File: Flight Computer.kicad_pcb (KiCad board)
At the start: 4 copper layers, 46 x 78.2 mm, 91 parts, among them J1 Conn_01x08, J2 JTAG, Q1 Q_PMOS_GDS, Q2 Q_NMOS_GDS, Q3 Q_NMOS_GDS, Q4 Q_NMOS_GDS, Q5 Q_PMOS_GDS, Q6 Q_PMOS_GDS, SW1 Reset, U1 VXO7803-1000, U2 W25Q16JVSS, U3 W25Q16JVSS, U4 Adafruit_GPS_THT, U5 ADXL345, U6 STM32F303RETx, U7 MAX7375AXR805, U8 BMP280

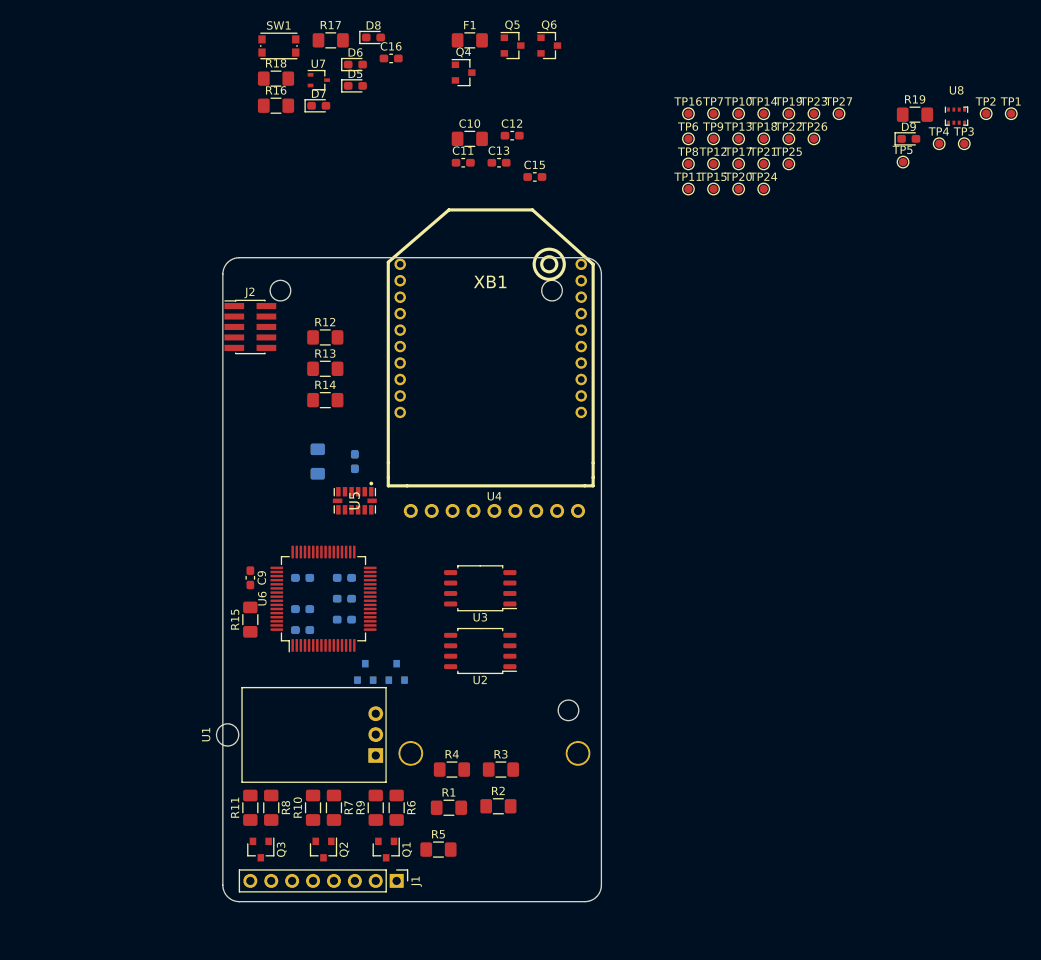
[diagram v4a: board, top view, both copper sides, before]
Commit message: Preliminary component placement
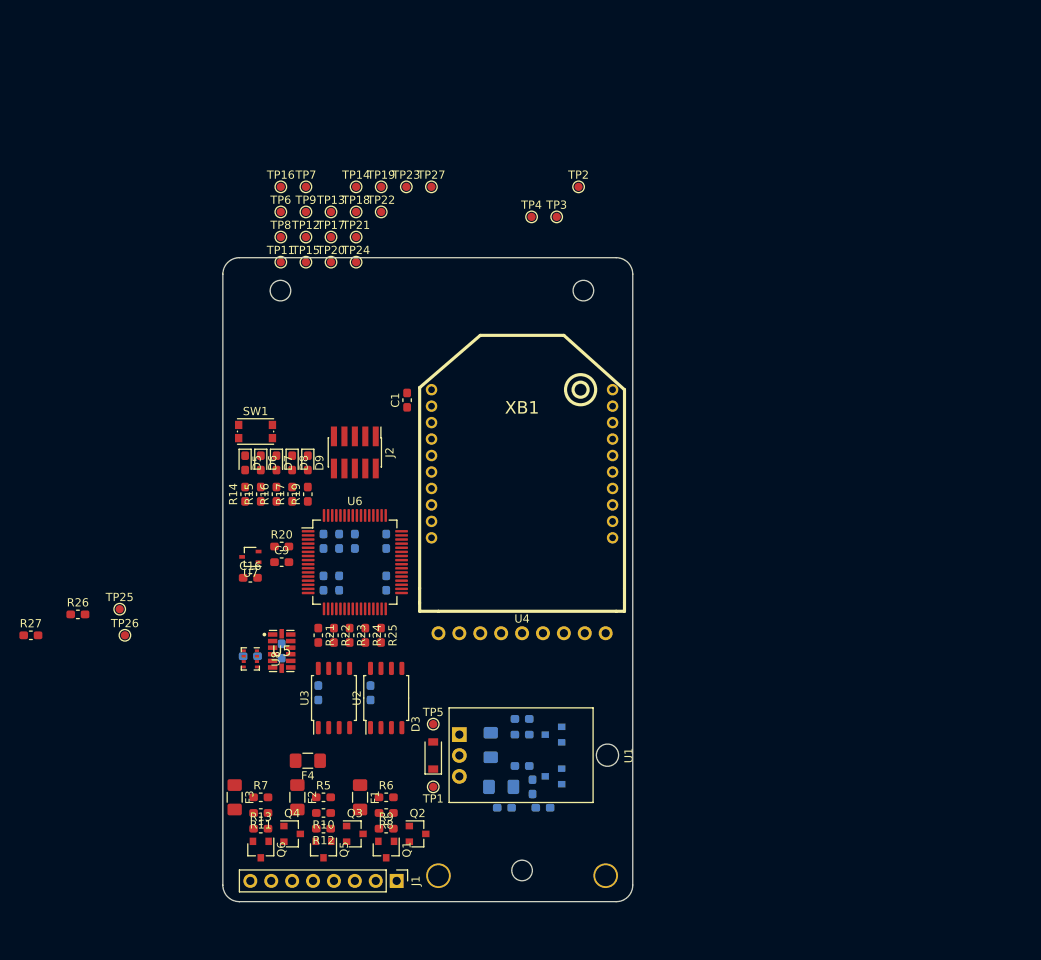
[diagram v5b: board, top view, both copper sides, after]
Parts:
- removed TP10: ACT4, TestPoint:TestPoint_Pad_D1.0mm
- added C14: 1n, Capacitor_SMD:C_0603_1608Metric_Pad1.05x0.95mm_HandSolder, B.Cu at (86.4, 111.8)
- added C17: 1n, Capacitor_SMD:C_0603_1608Metric_Pad1.05x0.95mm_HandSolder, B.Cu at (86.4, 106.0)
- added D3: BAT46, Diode_SMD:D_SOD-123, F.Cu at (75.6, 110.5)
- added F2: 1A Polyfuse, Fuse:Fuse_1206_3216Metric_Pad1.42x1.75mm_HandSolder, F.Cu at (59.1, 115.6)
- added F3: 1A Polyfuse, Fuse:Fuse_1206_3216Metric_Pad1.42x1.75mm_HandSolder, F.Cu at (51.4, 115.6)
- added F4: 3A Polyfuse, Fuse:Fuse_1206_3216Metric_Pad1.42x1.75mm_HandSolder, F.Cu at (60.3, 111.1)
- added R20: 10R, Resistor_SMD:R_0603_1608Metric_Pad1.05x0.95mm_HandSolder, F.Cu at (57.1, 85.1)
- added R21: 10R, Resistor_SMD:R_0603_1608Metric_Pad1.05x0.95mm_HandSolder, F.Cu at (61.6, 95.9)
- added R22: 10R, Resistor_SMD:R_0603_1608Metric_Pad1.05x0.95mm_HandSolder, F.Cu at (63.5, 95.9)
- added R23: 10R, Resistor_SMD:R_0603_1608Metric_Pad1.05x0.95mm_HandSolder, F.Cu at (65.4, 95.9)
- added R24: 10R, Resistor_SMD:R_0603_1608Metric_Pad1.05x0.95mm_HandSolder, F.Cu at (67.3, 95.9)
- added R25: 10R, Resistor_SMD:R_0603_1608Metric_Pad1.05x0.95mm_HandSolder, F.Cu at (69.2, 95.9)
- added R26: 2.2k, Resistor_SMD:R_0603_1608Metric_Pad1.05x0.95mm_HandSolder, F.Cu at (32.4, 93.3)
- added R27: 2.2k, Resistor_SMD:R_0603_1608Metric_Pad1.05x0.95mm_HandSolder, F.Cu at (26.7, 95.9)
- C1: moved to F.Cu
- C10, C11, C12, C13, C15: moved to B.Cu
- F1: value 3A Polyfuse -> 1A Polyfuse
- G1: footprint Flight-Computer:UB-SEDS-Logo -> Flight-Computer:SEDS_logo_soldermask
- R1, R18, R2, R3, R4: footprint Resistor_SMD:R_1206_3216Metric_Pad1.42x1.75mm_HandSolder -> Resistor_SMD:R_0603_1608Metric_Pad1.05x0.95mm_HandSolder; moved to B.Cu
- R10, R11, R12, R13, R5, R6, R7, R8, R9: footprint Resistor_SMD:R_1206_3216Metric_Pad1.42x1.75mm_HandSolder -> Resistor_SMD:R_0603_1608Metric_Pad1.05x0.95mm_HandSolder
- R14, R15, R16, R17, R19: value 1k -> 470R; footprint Resistor_SMD:R_1206_3216Metric_Pad1.42x1.75mm_HandSolder -> Resistor_SMD:R_0603_1608Metric_Pad1.05x0.95mm_HandSolder
- moved U8 108.2 mm to (53.3, 98.8), turned to 270 degrees
- moved TP1 107.8 mm to (75.6, 114.3), turned to 180 degrees
- moved Q6 103.8 mm to (54.6, 121.9), turned to 270 degrees
- moved TP26 103.2 mm to (38.1, 95.9)
- moved Q5 100.4 mm to (62.2, 121.9), turned to 270 degrees
- moved TP25 97.7 mm to (37.5, 92.7)
- moved Q4 94.8 mm to (58.4, 120.0)
- moved F1 92.9 mm to (66.7, 115.6), turned to 270 degrees
- moved TP5 89.0 mm to (75.6, 106.7)
- moved R19 87.0 mm to (60.3, 78.7), turned to 90 degrees
- moved D9 83.0 mm to (60.3, 74.9), turned to 270 degrees
- moved C10 73.7 mm to (82.5, 109.2), turned to 90 degrees
- moved C12 69.9 mm to (67.9, 102.9), turned to 90 degrees
- moved C13 68.1 mm to (61.6, 102.9), turned to 90 degrees
- moved C15 67.7 mm to (53.3, 98.4), turned to 180 degrees
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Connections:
- F1 pad 1: +BATT -> Net-(F1-Pad1)
- Q5 pad 2: Net-(F1-Pad2) -> Net-(F2-Pad2)
- Q6 pad 2: Net-(F1-Pad2) -> Net-(F3-Pad2)
- R12 pad 1: Net-(F1-Pad2) -> Net-(F2-Pad2)
- R13 pad 1: Net-(F1-Pad2) -> Net-(F3-Pad2)
- U6 pad 11: /ACT4 -> (no net)
- U6 pad 30: /SPI2_CS1 -> Net-(R21-Pad1)
- U6 pad 33: /SPI2_CS2 -> Net-(R24-Pad1)
- U6 pad 34: /SPI2_SCK -> Net-(R22-Pad1)
- U6 pad 35: /SPI2_MISO -> Net-(R25-Pad1)
- U6 pad 36: /SPI2_MOSI -> Net-(R23-Pad1)
- U6 pad 5: /MCU/OSC_IN -> Net-(R20-Pad2)
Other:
- board size 46 x 78.2 mm -> 49.8 x 78.2 mm
- board text added: "Flight Computer Rev 4"
- board text removed: "Flight Computer Rev 3"

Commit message: Much more compact component placement Some routing done
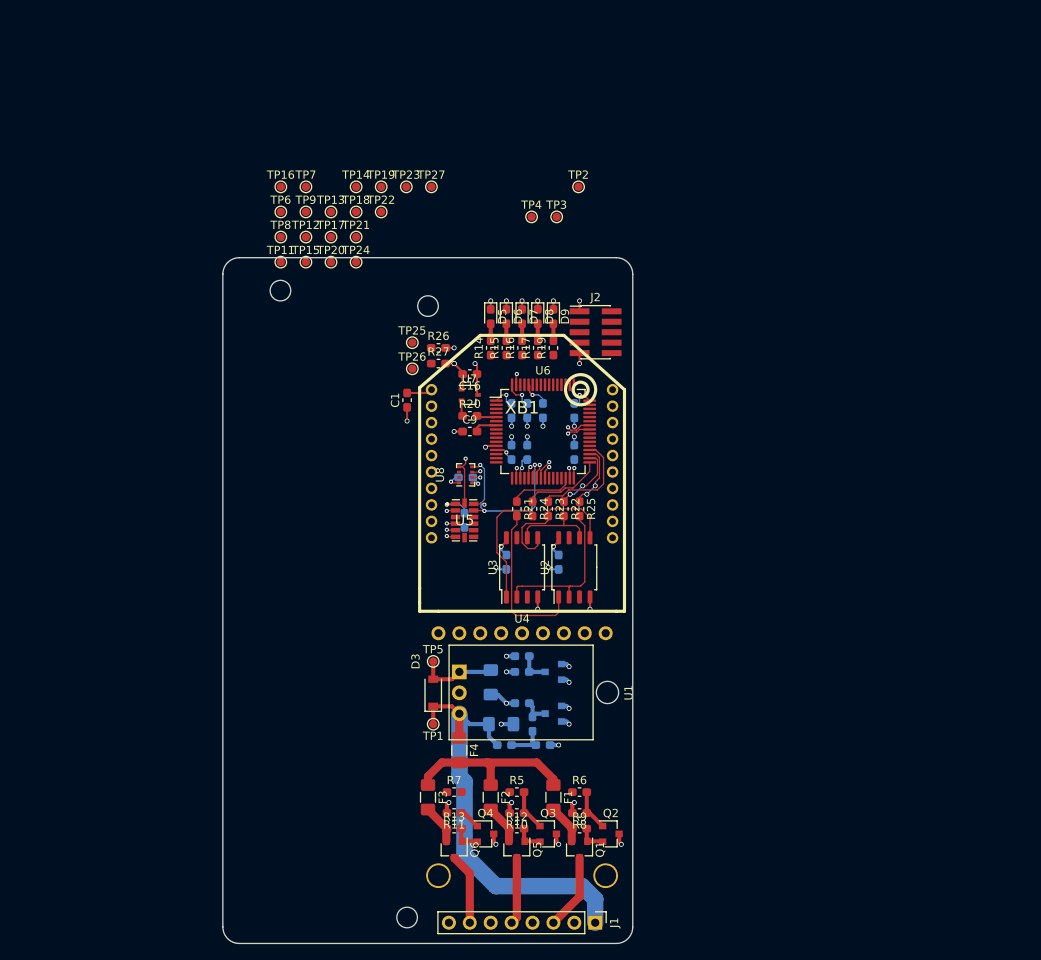
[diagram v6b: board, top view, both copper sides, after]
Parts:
- removed SW1: Reset, Button_Switch_SMD:SW_Push_1P1T_NO_CK_KMR2
- moved R27 59.5 mm to (76.2, 62.9)
- moved R26 54.5 mm to (76.2, 61.0)
- moved TP25 48.1 mm to (73.0, 60.3)
- moved TP26 47.6 mm to (73.0, 63.5)
- moved C16 36.4 mm to (80.0, 64.1), turned to 180 degrees
- moved D5 34.7 mm to (82.5, 57.1)
- moved D6 34.7 mm to (84.5, 57.1)
- moved D7 34.7 mm to (86.4, 57.1)
- moved D8 34.7 mm to (88.3, 57.1)
- moved D9 34.7 mm to (90.2, 57.1)
- moved R14 34.7 mm to (82.5, 61.0)
- moved R15 34.7 mm to (84.5, 61.0)
- moved R16 34.7 mm to (86.4, 61.0)
- moved R17 34.7 mm to (88.3, 61.0)
- moved R19 34.7 mm to (90.2, 61.0)
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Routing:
- net GND: track 0.00 -> 54.8 mm, vias 0 -> 41
- net +BATT: track 0.00 -> 54.1 mm
- net +3V3: track 0.00 -> 52.5 mm, vias 0 -> 19
- net /SPI1_MISO: track 0.00 -> 21.7 mm, vias 0 -> 3
- net Net-(F1-Pad1): track 0.00 -> 21.5 mm
- net /SPI2_CS1: track 0.00 -> 19.8 mm
- net /SPI2_MISO: track 0.00 -> 19.3 mm
- net /SPI2_MOSI: track 0.00 -> 17.8 mm
- net /SPI2_CS2: track 0.00 -> 15.4 mm
- net Net-(R23-Pad1): track 0.00 -> 13.2 mm
- net Net-(R24-Pad1): track 0.00 -> 10.4 mm
- net /SPI2_SCK: track 0.00 -> 10.0 mm
- net /DROGUE_POW: track 0.00 -> 9.21 mm
- net /AUX1_POW: track 0.00 -> 8.68 mm
- net Net-(R22-Pad1): track 0.00 -> 8.35 mm, vias 0 -> 2
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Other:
- board size 49.8 x 78.2 mm -> 49.8 x 83.3 mm
- net class Default: clearance 0.2 -> 0.089; trace_width 0.1524 -> 0.089
- rule trace_clearance: 0.2 -> 0.089
- rule trace_min: 0.1524 -> 0.089
- rule via_min_drill: 0.254 -> 0.2
- rule via_min_size: 0.508 -> 0.45

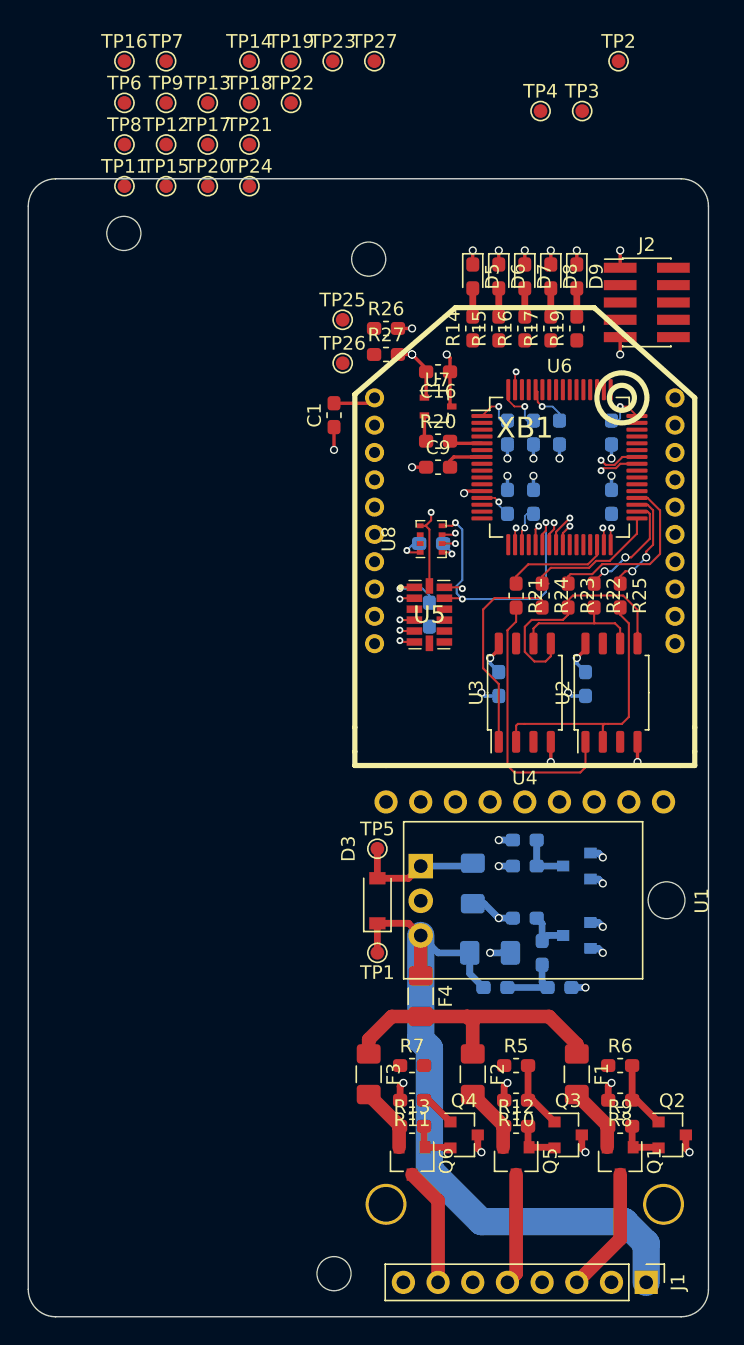
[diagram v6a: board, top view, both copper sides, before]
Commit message: Routing complete Removed some test points (couldn't easily place)
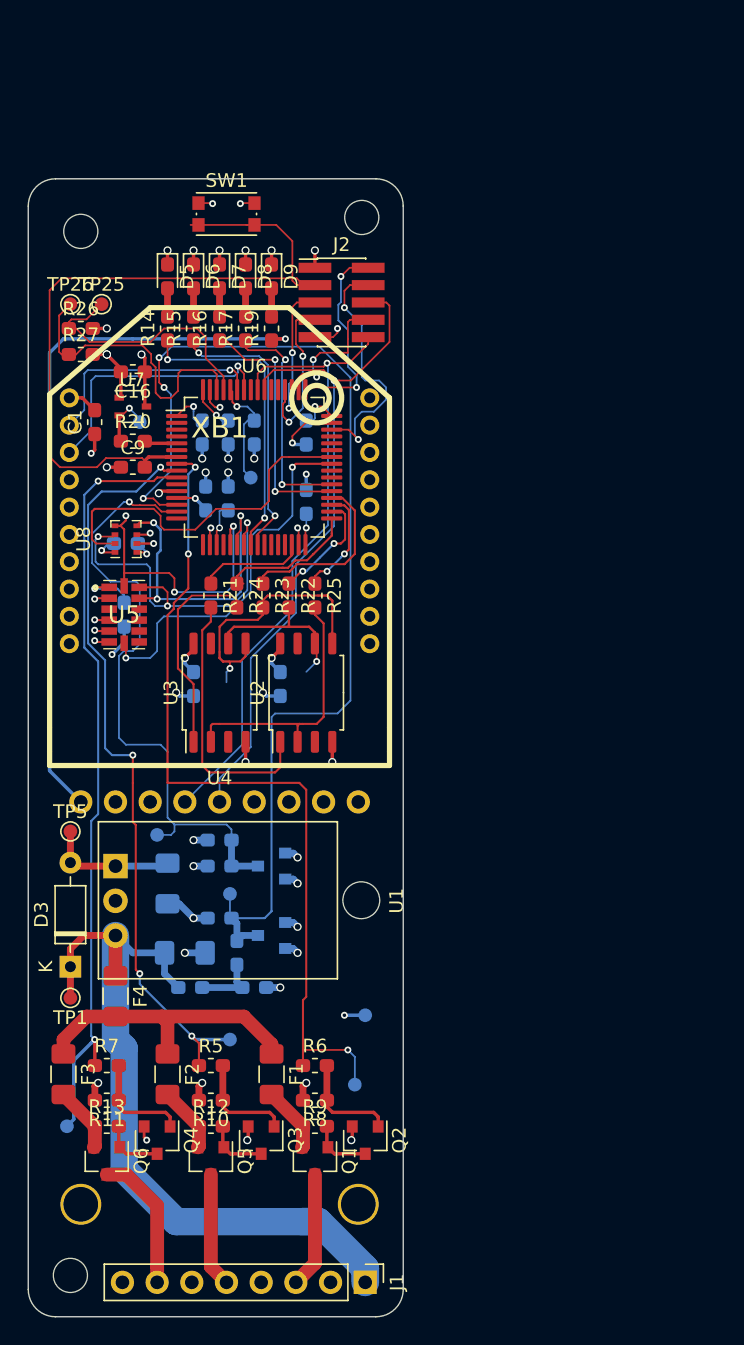
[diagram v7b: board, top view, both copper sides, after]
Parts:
- removed TP12: SPI2_CS1, TestPoint:TestPoint_Pad_D1.0mm
- removed TP13: SPI2_CS2, TestPoint:TestPoint_Pad_D1.0mm
- removed TP14: SPI2_SCK, TestPoint:TestPoint_Pad_D1.0mm
- removed TP15: SPI2_MISO, TestPoint:TestPoint_Pad_D1.0mm
- removed TP16: SPI2_MOSI, TestPoint:TestPoint_Pad_D1.0mm
- removed TP17: USART1_RX, TestPoint:TestPoint_Pad_D1.0mm
- removed TP18: SPI1_CS1, TestPoint:TestPoint_Pad_D1.0mm
- removed TP19: USART1_TX, TestPoint:TestPoint_Pad_D1.0mm
- removed TP20: SPI1_CS2, TestPoint:TestPoint_Pad_D1.0mm
- removed TP21: USART2_RX, TestPoint:TestPoint_Pad_D1.0mm
- removed TP22: SPI1_SCK, TestPoint:TestPoint_Pad_D1.0mm
- removed TP23: USART2_TX, TestPoint:TestPoint_Pad_D1.0mm
- removed TP24: SPI1_MISO, TestPoint:TestPoint_Pad_D1.0mm
- removed TP27: SPI1_MOSI, TestPoint:TestPoint_Pad_D1.0mm
- added SW1: Reset, Button_Switch_SMD:SW_Push_1P1T_NO_CK_KMR2, F.Cu at (64.5, 52.6)
- D3: footprint Diode_SMD:D_SOD-123 -> Diode_THT:D_DO-35_SOD27_P7.62mm_Horizontal
- Q1, Q5, Q6: value Q_PMOS_GDS -> DMP3099
- Q2, Q3, Q4: value Q_NMOS_GDS -> 2N7002
- TP11, TP2, TP3, TP4, TP6, TP7, TP8, TP9: moved to B.Cu
- moved TP7 76.2 mm to (73.9, 116.3)
- moved TP9 75.3 mm to (52.8, 119.4)
- moved TP4 67.4 mm to (74.7, 111.3)
- moved TP2 67.3 mm to (64.8, 102.4)
- moved TP8 66.0 mm to (64.8, 113.0)
- moved TP3 61.5 mm to (59.4, 98.0)
- moved G1 26.1 mm to (92.5, 107.2)
- moved TP6 23.4 mm to (58.2, 67.8)
- moved TP11 23.3 mm to (66.3, 71.9)
- moved D3 23.0 mm to (53.1, 107.7)
- moved TP1 22.7 mm to (53.1, 110.0)
- moved TP5 22.5 mm to (53.1, 97.8)
- moved Q4 22.5 mm to (59.4, 120.4), turned to 270 degrees
- moved Q2 22.5 mm to (74.7, 120.4), turned to 270 degrees
- moved Q3 22.5 mm to (67.1, 120.4), turned to 270 degrees
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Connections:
- Q2 pad 2: Net-(Q1-Pad1) -> GND
- Q2 pad 3: GND -> Net-(Q1-Pad1)
- Q3 pad 2: Net-(Q3-Pad2) -> GND
- Q3 pad 3: GND -> Net-(Q3-Pad3)
- Q4 pad 2: Net-(Q4-Pad2) -> GND
- Q4 pad 3: GND -> Net-(Q4-Pad3)
- Q5 pad 1: Net-(Q3-Pad2) -> Net-(Q3-Pad3)
- Q6 pad 1: Net-(Q4-Pad2) -> Net-(Q4-Pad3)
- R12 pad 2: Net-(Q3-Pad2) -> Net-(Q3-Pad3)
- R13 pad 2: Net-(Q4-Pad2) -> Net-(Q4-Pad3)
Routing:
- net /ADC1: track 3.53 -> 82.1 mm, vias 0 -> 3
- net /ACT1: track 0.00 -> 62.1 mm, vias 0 -> 3
- net /ACT3: track 0.00 -> 57.0 mm, vias 0 -> 2
- net /ACT2: track 0.00 -> 55.9 mm, vias 0 -> 4
- net Net-(R19-Pad1): track 0.00 -> 52.6 mm, vias 0 -> 1
- net /MCU/NRST: track 2.93 -> 55.4 mm
- net /USART2_TX: track 0.00 -> 50.3 mm, vias 0 -> 1
- net /USART2_RX: track 0.00 -> 47.2 mm, vias 0 -> 1
- net /ADC2: track 3.84 -> 46.8 mm, vias 0 -> 1
- net /SPI1_CS1: track 2.84 -> 27.8 mm, vias 1 -> 2
- net /SPI1_MOSI: track 3.11 -> 27.5 mm, vias 2 -> 3
- net /SPI1_CS2: track 3.01 -> 26.1 mm, vias 1 -> 0
- net /MCU/I2C1_SCL: track 0.00 -> 21.6 mm
- net Net-(R14-Pad1): track 2.37 -> 22.2 mm, vias 1 -> 2
- net /USART1_TX: track 0.00 -> 19.3 mm, vias 0 -> 1
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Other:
- board size 49.8 x 83.3 mm -> 27.5 x 83.3 mm
- net class Default: clearance 0.089 -> 0.127; trace_width 0.089 -> 0.127
- rule solder_mask_min_width: 0.25 -> 0.1016
- rule trace_clearance: 0.089 -> 0.127
- rule trace_min: 0.089 -> 0.127
- rule via_min_drill: 0.2 -> 0.254
- rule via_min_size: 0.45 -> 0.4572
